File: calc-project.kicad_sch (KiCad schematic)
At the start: 39 parts, among them J1 PinSocket_1x20_Right, J2 PinSocket_1x20_Left, J3 Conn_01x14, SW1 SW_Push_45deg, SW10 SW_Push_45deg, SW11 SW_Push_45deg, SW12 SW_Push_45deg, SW13 SW_Push_45deg, SW14 SW_Push_45deg, SW15 SW_Push_45deg, SW16 SW_Push_45deg, SW17 SW_Push_45deg, SW18 SW_Push_45deg, SW19 SW_Push_45deg, SW2 SW_Push_45deg, SW20 SW_Push_45deg, SW21 SW_Push_45deg, SW22 SW_Push_45deg, SW23 SW_Push_45deg, SW24 SW_Push_45deg, SW25 SW_Push_45deg, SW26 SW_Push_45deg, SW27 SW_Push_45deg, SW28 SW_Push_45deg, SW29 SW_Push_45deg, SW3 SW_Push_45deg, SW30 SW_Push_45deg, SW31 SW_Push_45deg, SW32 SW_Push_45deg, SW33 SW_Push_45deg, SW34 SW_Push_45deg, SW35 SW_Push_45deg, SW36 SW_Push_45deg, SW4 SW_Push_45deg, SW5 SW_Push_45deg, SW6 SW_Push_45deg, SW7 SW_Push_45deg, SW8 SW_Push_45deg, SW9 SW_Push_45deg

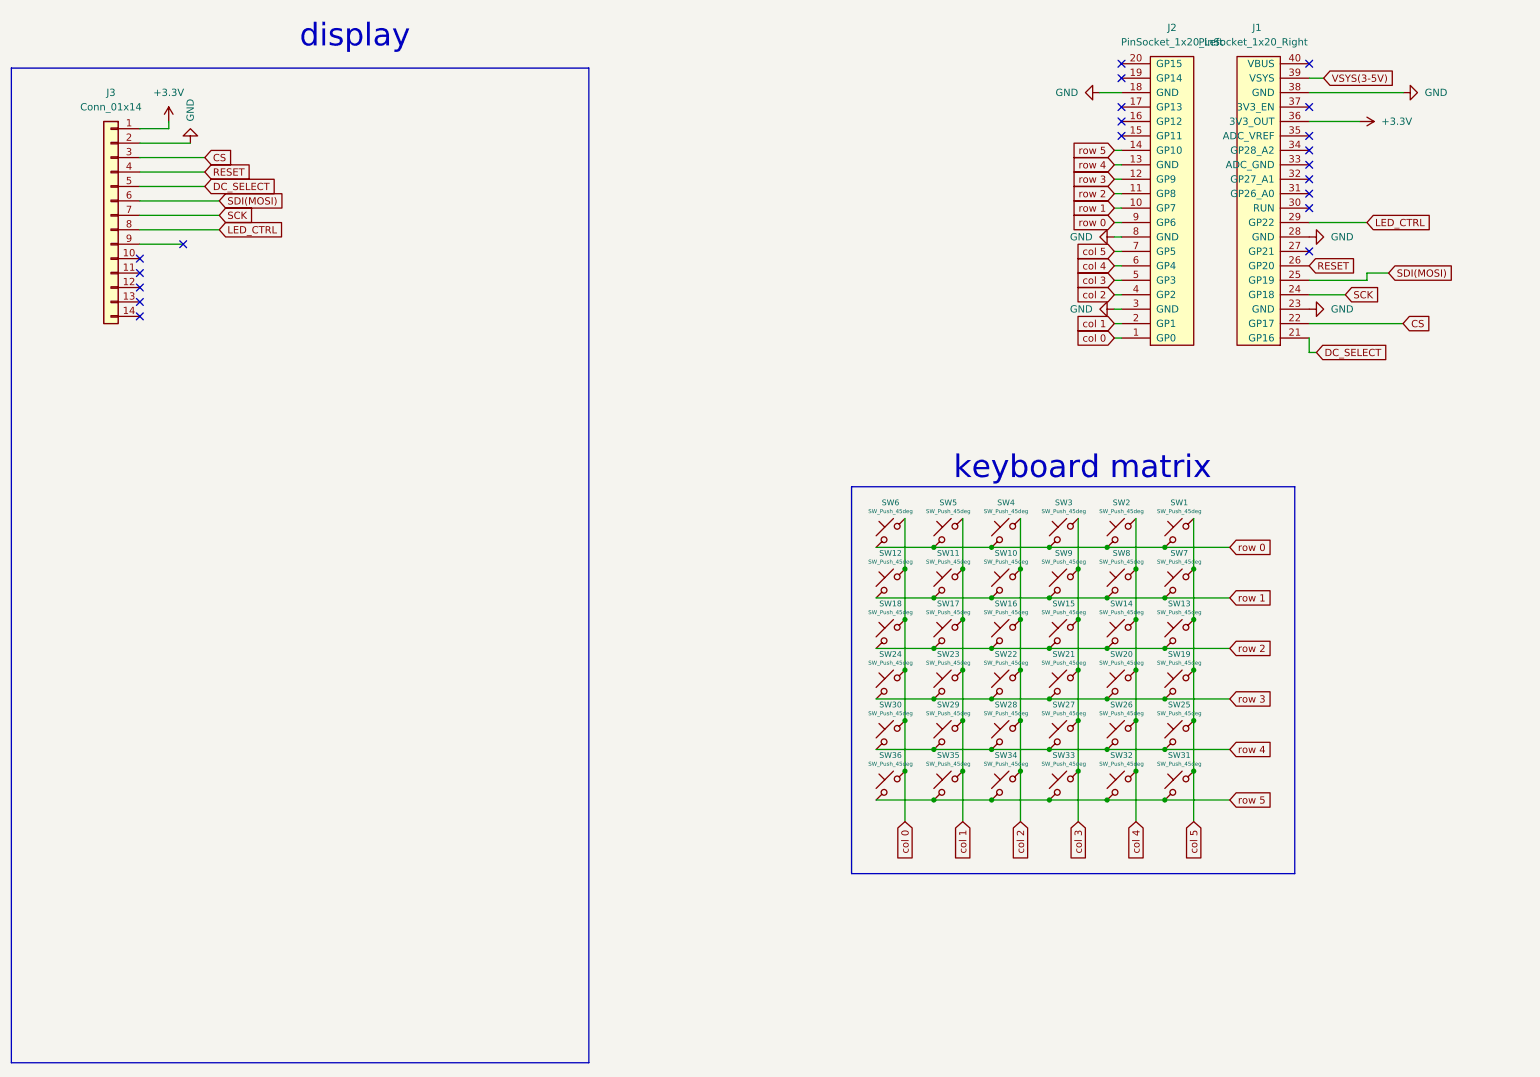
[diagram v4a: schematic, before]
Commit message: edited some stuff
fixed footprint, wired up, moved screen
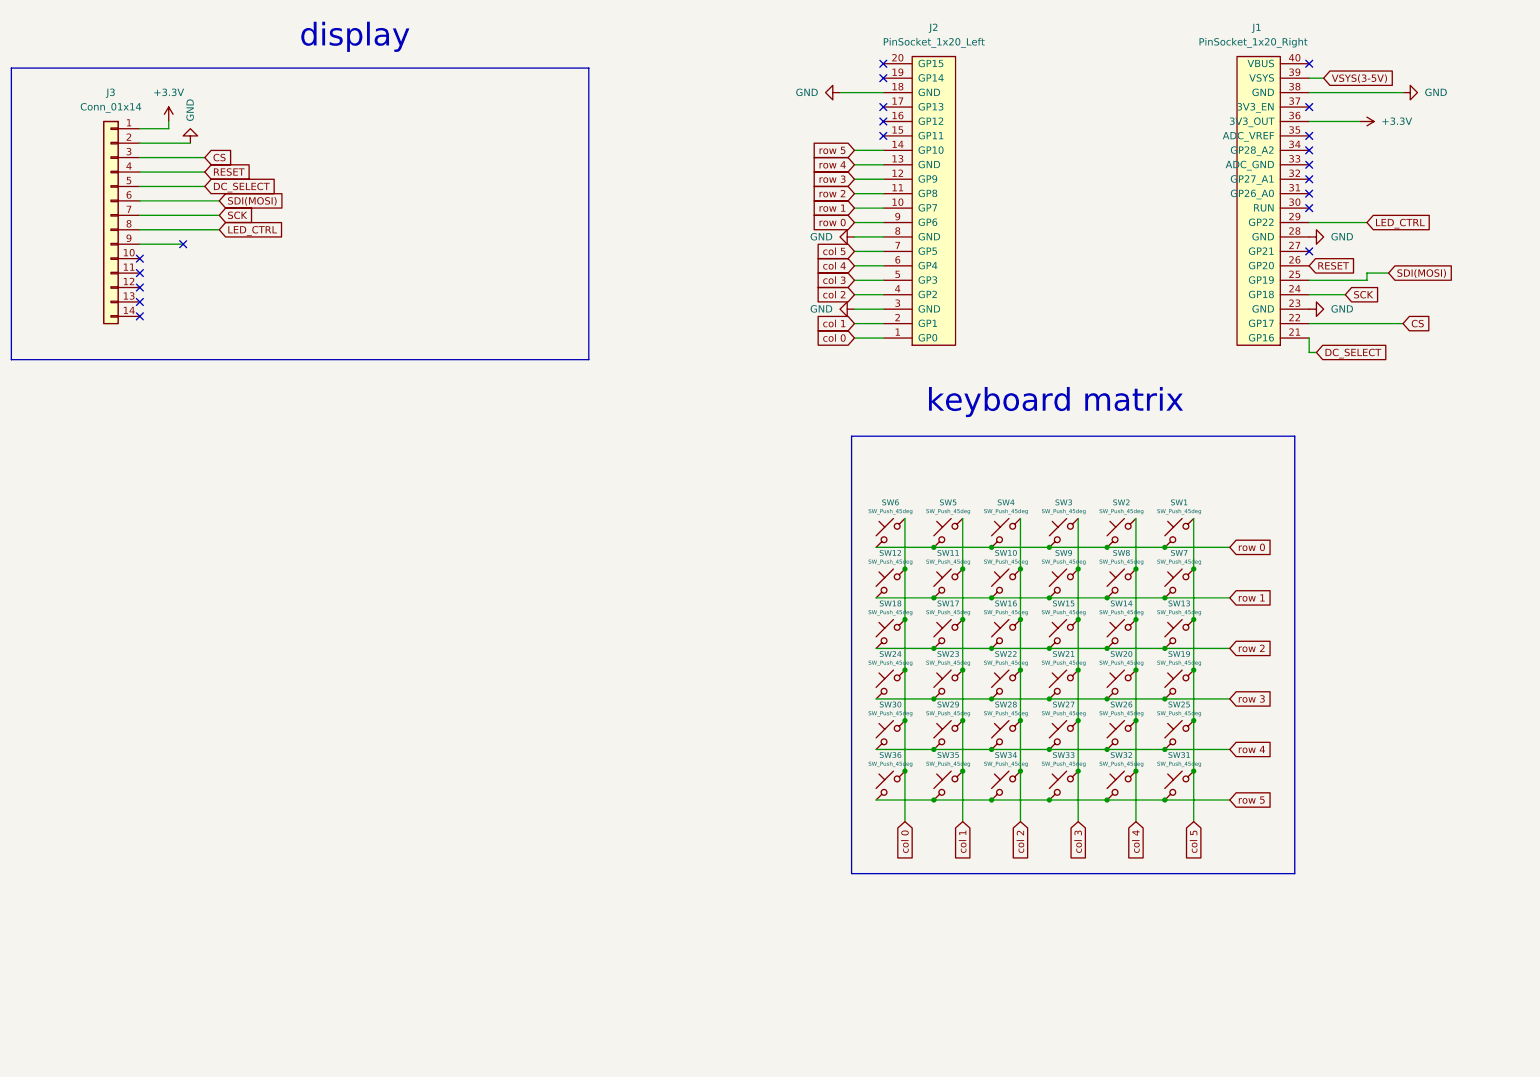
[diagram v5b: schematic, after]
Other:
- moved on the sheet: J2

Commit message: routing
routing
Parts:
- SW1, SW10, SW11, SW12, SW13, SW14, SW15, SW16, SW17, SW18, SW19, SW2, SW20, SW21, SW22, SW23, SW24, SW25, SW26, SW27, SW28, SW29, SW3, SW30, SW31, SW32, SW33, SW34, SW35, SW36, SW4, SW5, SW6, SW7, SW8, SW9: footprint Library:SW_TL3315NF160Q -> Library:SW_PUSH_6mm_centered
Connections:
- net GND: no longer J1.28 (GND), J1.38 (GND), J2.18 (GND), J2.3 (GND), J2.8 (GND)
- net VSYS(3-5V): no longer names the net of J1.39 (VSYS)
- no-connect marks 20 -> 26

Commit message: capabilities
yeah
did use kicad happy just to check and make sure we had capabilities
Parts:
- J1, J2: KiLib_Generator (none) -> connector/pin_header_socket
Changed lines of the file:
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@@
+			)
+		)
+		(property "KiLib_Generator" "connector/pin_header_socket"
+			(at 173.99 45.72 0)
+			(hide yes)
+			(show_name no)
+			(do_not_autoplace no)
+			(effects
+				(font
+					(size 1.27 1.27)
+				)
 			)
 		)
@@
 			(at 231.14 45.72 0)
 			(hide yes)
+			(show_name no)
+			(do_not_autoplace no)
+			(effects
+				(font
+					(size 1.27 1.27)
+				)
+			)
+		)
+		(property "KiLib_Generator" "connector/pin_header_socket"
+			(at 231.14 45.72 0)
+			(hide yes)

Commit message: wrong pin
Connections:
- net row 4: now also J2.14 (GP10); no longer J2.13 (GND)
- net row 5: now also J2.15 (GP11); no longer J2.14 (GP10)
